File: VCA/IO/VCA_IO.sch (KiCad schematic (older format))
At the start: 15 parts, among them J1 Out_B, J10 IO_B, J11 Power, J2 CV1_B, J3 In_B, J4 CV2_B, J5 IO_A, J6 CV1_A, J7 In_A, J8 CV2_A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

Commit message: Bunch of bug fixes and tweaks
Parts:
- added H1: Top_MH1, Eurorack:eurorack_mounting_hole, symbol Mechanical:MountingHole_Pad
- added H2: Bottom_MH1, Eurorack:eurorack_mounting_hole, symbol Mechanical:MountingHole_Pad
- added H3: Top_MH2, Eurorack:eurorack_mounting_hole, symbol Mechanical:MountingHole_Pad
- added H4: Bottom_MH2, Eurorack:eurorack_mounting_hole, symbol Mechanical:MountingHole_Pad
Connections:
- net GNDREF: now also H1.1, H2.1, H3.1, H4.1
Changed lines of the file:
@@
 EESchema Schematic File Version 4
-LIBS:AS3360_VCA-cache
-EELAYER 29 0
+LIBS:VCA_IO-cache
+EELAYER 30 0
 EELAYER END
 $Descr A4 11693 8268
@@
 Wire Wire Line
 	8800 2950 8800 3300
+$Comp
+L Mechanical:MountingHole_Pad H1
+U 1 1 5D9303C3
+P 8650 950
+F 0 "H1" H 8750 999 50  0000 L CNN
+F 1 "Top_MH1" H 8750 908 50  0000 L CNN
+F 2 "Eurorack:eurorack_mounting_hole" H 8650 950 50  0001 C CNN
+F 3 "~" H 8650 950 50  0001 C CNN
+	1    8650 950
+	1    0    0    -1
+$EndComp
+$Comp
+L power:GNDREF #PWR0109
+U 1 1 5D930ACE
+P 8650 1050
+F 0 "#PWR0109" H 8650 800 50  0001 C CNN
+F 1 "GNDREF" H 8655 877 50  0001 C CNN
+F 2 "" H 8650 1050 50  0001 C CNN
+F 3 "" H 8650 1050 50  0001 C CNN
+	1    8650 1050
+	1    0    0    -1
+$EndComp
+$Comp
+L Mechanical:MountingHole_Pad H3
+U 1 1 5D931B86
+P 9700 950
+F 0 "H3" H 9800 999 50  0000 L CNN
+F 1 "Top_MH2" H 9800 908 50  0000 L CNN
+F 2 "Eurorack:eurorack_mounting_hole" H 9700 950 50  0001 C CNN
+F 3 "~" H 9700 950 50  0001 C CNN
+	1    9700 950
+	1    0    0    -1
+$EndComp
+$Comp
+L power:GNDREF #PWR0115
+U 1 1 5D931B8C
+P 9700 1050
+F 0 "#PWR0115" H 9700 800 50  0001 C CNN
+F 1 "GNDREF" H 9705 877 50  0001 C CNN
+F 2 "" H 9700 1050 50  0001 C CNN
+F 3 "" H 9700 1050 50  0001 C CNN
+	1    9700 1050
+	1    0    0    -1
+$EndComp
+$Comp
+L Mechanical:MountingHole_Pad H2
+U 1 1 5D9344C5
+P 8650 1450
+F 0 "H2" H 8750 1499 50  0000 L CNN
+F 1 "Bottom_MH1" H 8750 1408 50  0000 L CNN
+F 2 "Eurorack:eurorack_mounting_hole" H 8650 1450 50  0001 C CNN
+F 3 "~" H 8650 1450 50  0001 C CNN
+	1    8650 1450
+	1    0    0    -1
+$EndComp
+$Comp
+L power:GNDREF #PWR0116
+U 1 1 5D9344CB
+P 8650 1550
+F 0 "#PWR0116" H 8650 1300 50  0001 C CNN
+F 1 "GNDREF" H 8655 1377 50  0001 C CNN
+F 2 "" H 8650 1550 50  0001 C CNN
+F 3 "" H 8650 1550 50  0001 C CNN
+	1    8650 1550
+	1    0    0    -1
+$EndComp
+$Comp
+L Mechanical:MountingHole_Pad H4
+U 1 1 5D93697C
+P 9700 1450
+F 0 "H4" H 9800 1499 50  0000 L CNN
+F 1 "Bottom_MH2" H 9800 1408 50  0000 L CNN
+F 2 "Eurorack:eurorack_mounting_hole" H 9700 1450 50  0001 C CNN
+F 3 "~" H 9700 1450 50  0001 C CNN
+	1    9700 1450
+	1    0    0    -1
+$EndComp
+$Comp
+L power:GNDREF #PWR0117
+U 1 1 5D936982
+P 9700 1550
+F 0 "#PWR0117" H 9700 1300 50  0001 C CNN
+F 1 "GNDREF" H 9705 1377 50  0001 C CNN
+F 2 "" H 9700 1550 50  0001 C CNN
+F 3 "" H 9700 1550 50  0001 C CNN
+	1    9700 1550
+	1    0    0    -1
+$EndComp
 $EndSCHEMATC

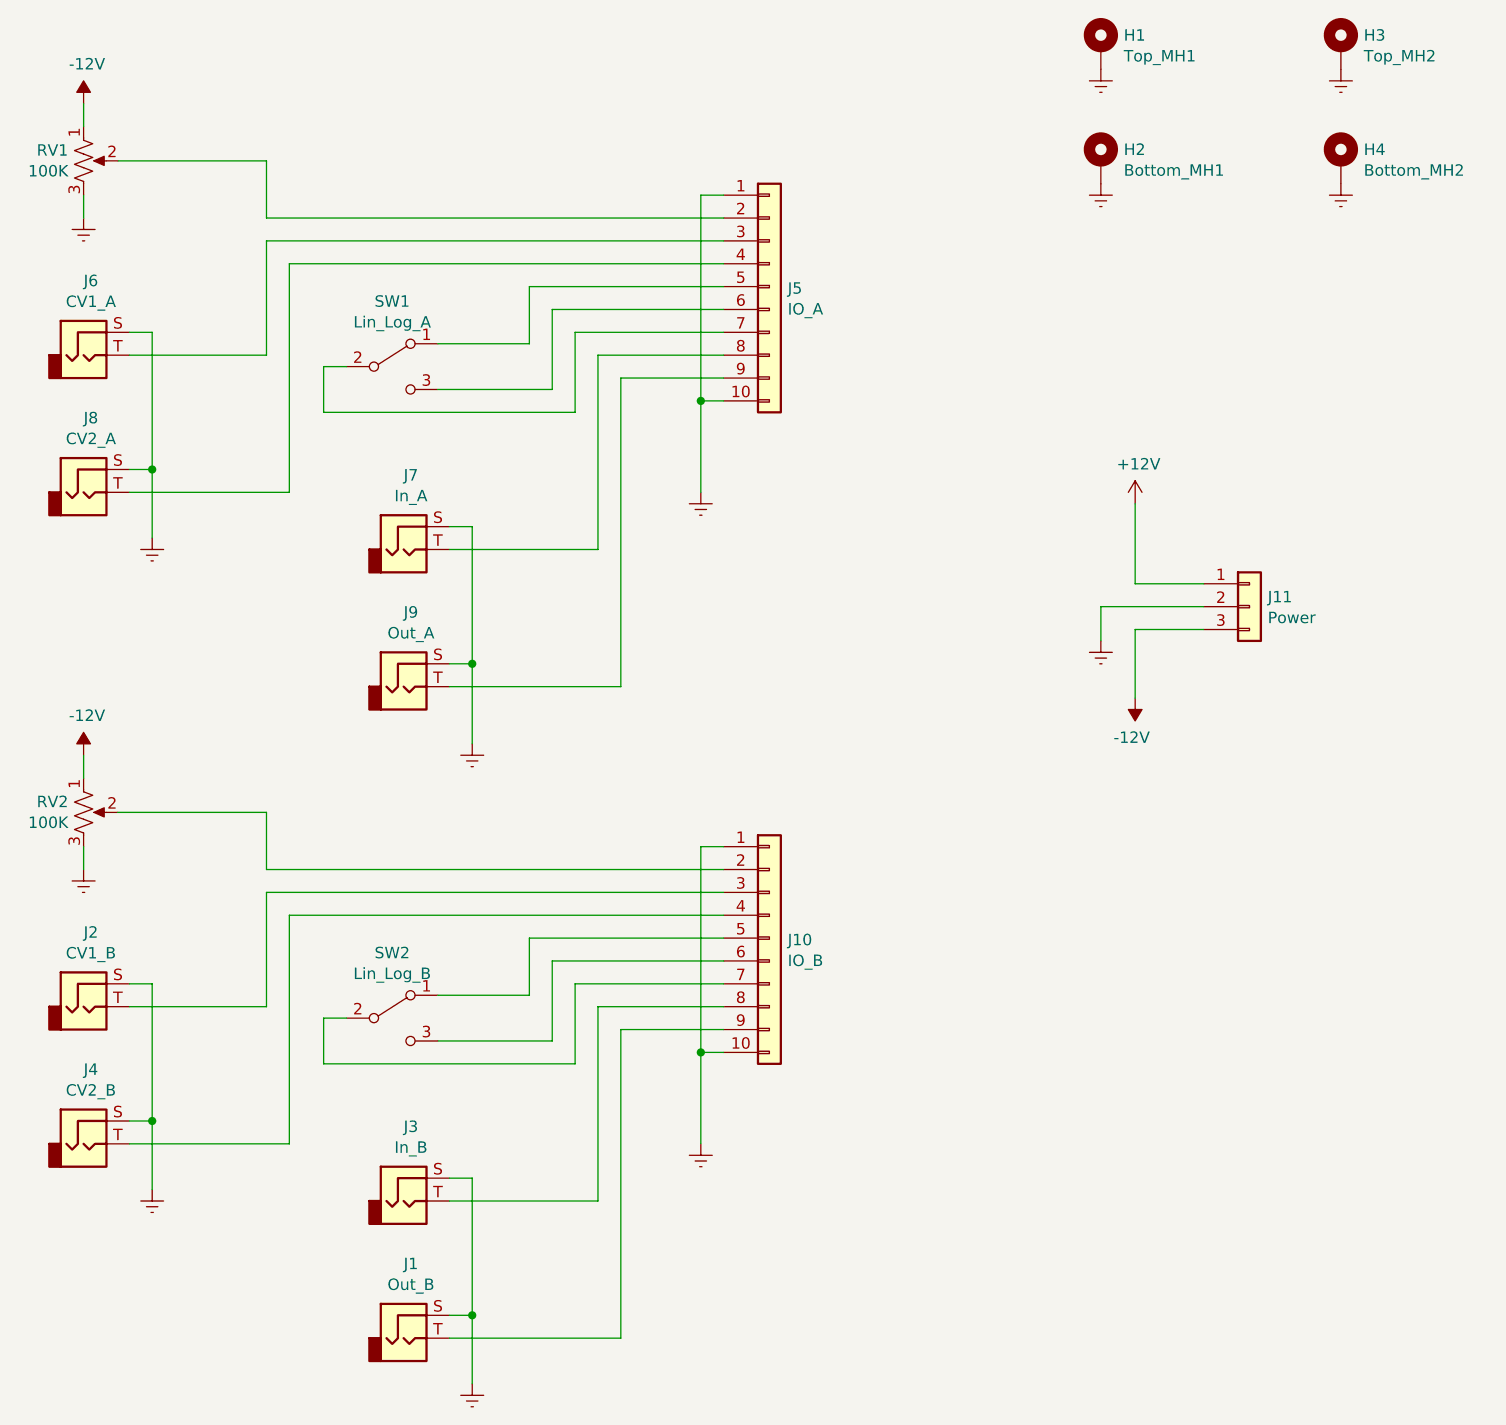
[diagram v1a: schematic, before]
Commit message: Clean up layout of VCA board
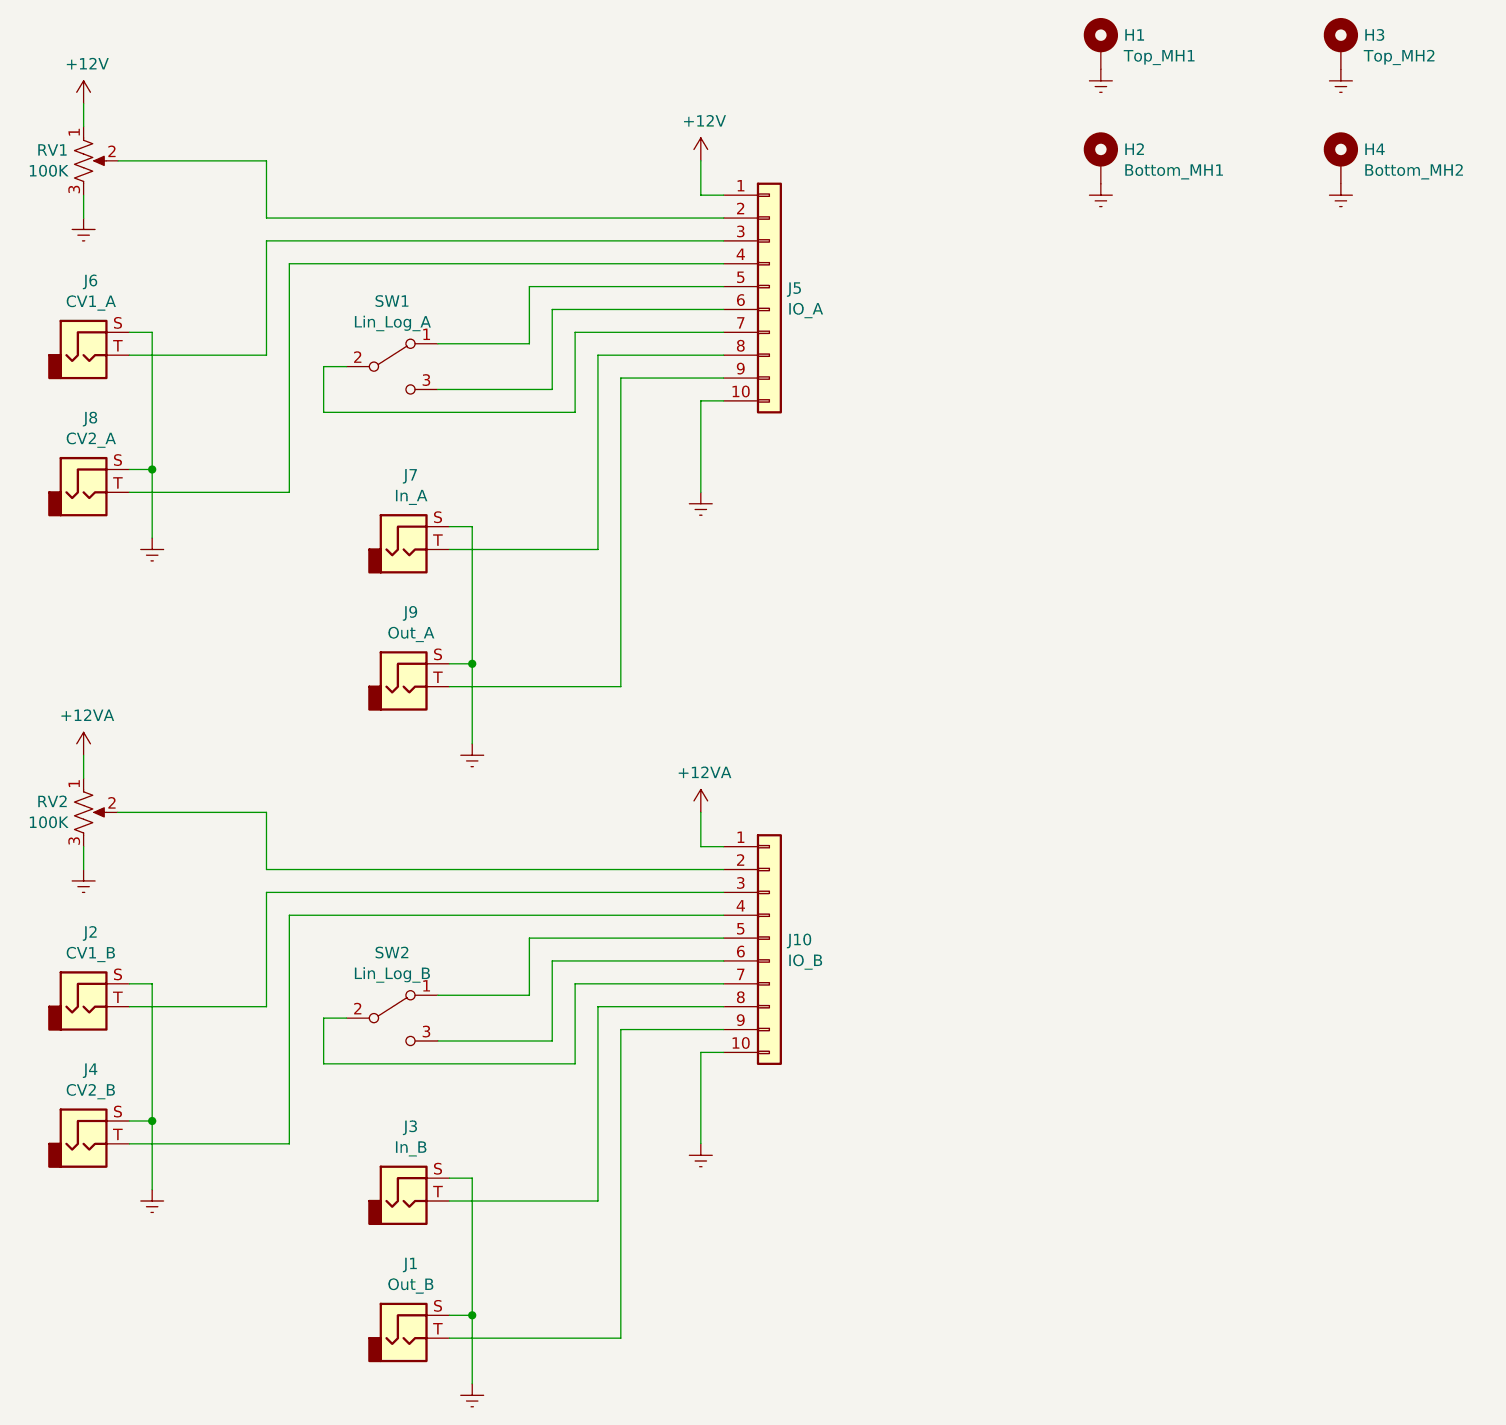
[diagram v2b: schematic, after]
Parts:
- removed J11: Power, Connector_PinSocket_2.54mm:PinSocket_1x03_P2.54mm_Vertical, symbol Connector_Generic:Conn_01x03
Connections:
- net +12V: now also J5.1 (Pin_1), RV1.1
- net GNDREF: no longer J10.1 (Pin_1), J5.1 (Pin_1)
- net -12V renamed +12VA
- net +12VA: now also J10.1 (Pin_1); no longer RV1.1
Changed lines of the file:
@@
 Wire Wire Line
 	4200 1700 4200 1600
-$Comp
-L power:-12V #PWR0102
-U 1 1 5D7C32F9
-P 4200 1200
-F 0 "#PWR0102" H 4200 1300 50  0001 C CNN
-F 1 "-12V" H 4215 1373 50  0000 C CNN
-F 2 "" H 4200 1200 50  0001 C CNN
-F 3 "" H 4200 1200 50  0001 C CNN
-	1    4200 1200
-	1    0    0    -1
-$EndComp
 Wire Wire Line
 	4200 1200 4200 1300
@@
 	1    0    0    -1
 $EndComp
-$Comp
-L power:-12V #PWR0104
-U 1 1 5D7C3EA8
-P 4200 4050
-F 0 "#PWR0104" H 4200 4150 50  0001 C CNN
-F 1 "-12V" H 4215 4223 50  0000 C CNN
-F 2 "" H 4200 4050 50  0001 C CNN
-F 3 "" H 4200 4050 50  0001 C CNN
-	1    4200 4050
-	1    0    0    -1
-$EndComp
-$Comp
-L power:+12V #PWR0106
-U 1 1 5D7C6DCC
-P 8800 2950
-F 0 "#PWR0106" H 8800 2800 50  0001 C CNN
-F 1 "+12V" H 8815 3123 50  0000 C CNN
-F 2 "" H 8800 2950 50  0001 C CNN
-F 3 "" H 8800 2950 50  0001 C CNN
-	1    8800 2950
-	1    0    0    -1
-$EndComp
 Wire Wire Line
 	4200 4450 4200 4550
@@
 	6900 1600 7000 1600
 Wire Wire Line
-	9100 3500 8800 3500
-Wire Wire Line
-	8800 3500 8800 3800
-$Comp
-L power:-12V #PWR0105
-U 1 1 5D8742CF
-P 8800 3800
-F 0 "#PWR0105" H 8800 3900 50  0001 C CNN
-F 1 "-12V" H 8815 3973 50  0000 C CNN
-F 2 "" H 8800 3800 50  0001 C CNN
-F 3 "" H 8800 3800 50  0001 C CNN
-	1    8800 3800
-	-1   0    0    1
-$EndComp
-Wire Wire Line
 	4350 4300 5000 4300
 Wire Wire Line
@@
 Connection ~ 5900 6500
 $Comp
-L Connector_Generic:Conn_01x03 J11
-U 1 1 5D8D6E2F
-P 9300 3400
-F 0 "J11" H 9380 3442 50  0000 L CNN
-F 1 "Power" H 9380 3351 50  0000 L CNN
-F 2 "Connector_PinSocket_2.54mm:PinSocket_1x03_P2.54mm_Vertical" H 9300 3400 50  0001 C CNN
-F 3 "~" H 9300 3400 50  0001 C CNN
-	1    9300 3400
-	1    0    0    -1
-$EndComp
-$Comp
 L Connector_Generic:Conn_01x10 J5
 U 1 1 5D8DEBA8
@@
 	1    0    0    -1
 $EndComp
-Connection ~ 6900 2500
-Wire Wire Line
-	6900 2500 6900 1600
 Wire Wire Line
 	6900 2500 6900 2900
@@
 	1    0    0    -1
 $EndComp
-Connection ~ 6900 5350
-Wire Wire Line
-	6900 5350 6900 4450
 Wire Wire Line
 	6900 5350 6900 5750
@@
 $EndComp
 $Comp
-L power:GNDREF #PWR0108
-U 1 1 5D907247
-P 8650 3550
-F 0 "#PWR0108" H 8650 3300 50  0001 C CNN
-F 1 "GNDREF" H 8655 3377 50  0001 C CNN
-F 2 "" H 8650 3550 50  0001 C CNN
-F 3 "" H 8650 3550 50  0001 C CNN
-	1    8650 3550
-	1    0    0    -1
-$EndComp
-Wire Wire Line
-	8650 3550 8650 3400
-Wire Wire Line
-	8650 3400 9100 3400
-Wire Wire Line
-	8800 3300 9100 3300
-Wire Wire Line
-	8800 2950 8800 3300
-$Comp
 L Mechanical:MountingHole_Pad H1
 U 1 1 5D9303C3
@@
 	1    0    0    -1
 $EndComp
+$Comp
+L power:+12V #PWR0102
+U 1 1 5D9DB15B
+P 4200 1200
+F 0 "#PWR0102" H 4200 1050 50  0001 C CNN
+F 1 "+12V" H 4215 1373 50  0000 C CNN
+F 2 "" H 4200 1200 50  0001 C CNN
+F 3 "" H 4200 1200 50  0001 C CNN
+	1    4200 1200
+	1    0    0    -1
+$EndComp
+Wire Wire Line
+	6900 4450 6900 4300
+$Comp
+L power:+12V #PWR0106
+U 1 1 5D9E4A91
+P 6900 1450
+F 0 "#PWR0106" H 6900 1300 50  0001 C CNN
+F 1 "+12V" H 6915 1623 50  0000 C CNN
+F 2 "" H 6900 1450 50  0001 C CNN
+F 3 "" H 6900 1450 50  0001 C CNN
+	1    6900 1450
+	1    0    0    -1
+$EndComp
+Wire Wire Line
+	6900 1450 6900 1600
+$Comp
+L power:+12VA #PWR?
+U 1 1 5D9F3DB9
+P 6900 4300
+F 0 "#PWR?" H 6900 4150 50  0001 C CNN
+F 1 "+12VA" H 6915 4473 50  0000 C CNN
+F 2 "" H 6900 4300 50  0001 C CNN
+F 3 "" H 6900 4300 50  0001 C CNN
+	1    6900 4300
+	1    0    0    -1
+$EndComp
+$Comp
+L power:+12VA #PWR?
+U 1 1 5D9F9FC1
+P 4200 4050
+F 0 "#PWR?" H 4200 3900 50  0001 C CNN
+F 1 "+12VA" H 4215 4223 50  0000 C CNN
+F 2 "" H 4200 4050 50  0001 C CNN
+F 3 "" H 4200 4050 50  0001 C CNN
+	1    4200 4050
+	1    0    0    -1
+$EndComp

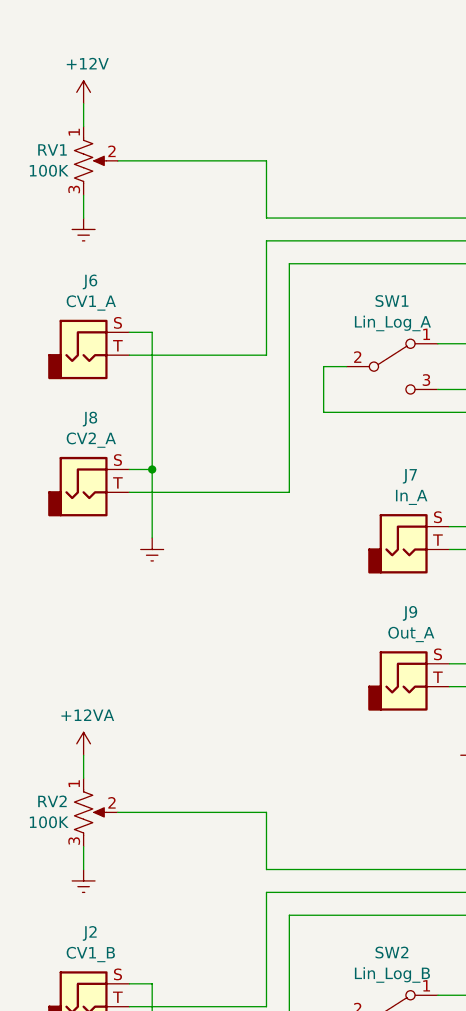
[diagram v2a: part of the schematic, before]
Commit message: Fix backwards knobs
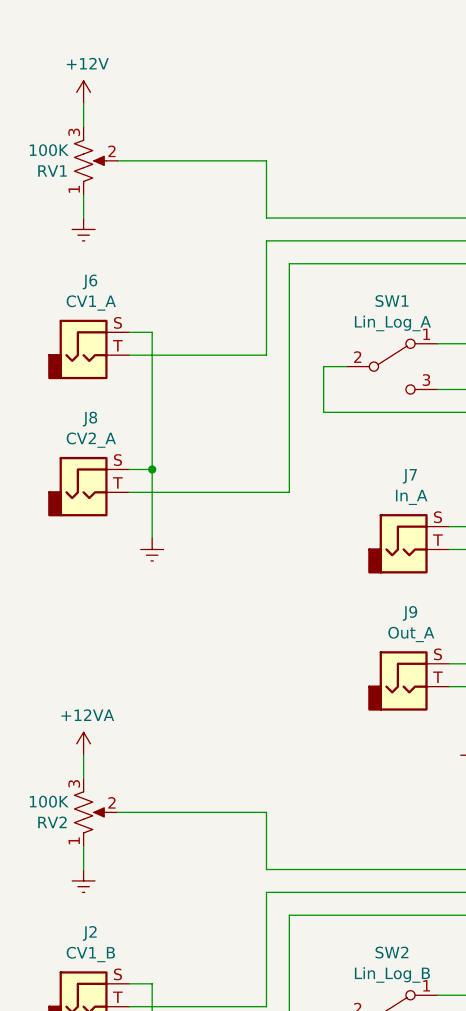
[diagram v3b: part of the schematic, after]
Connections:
- net +12V: now also RV1.3; no longer RV1.1
- net +12VA: now also RV2.3; no longer RV2.1
- net GNDREF: now also RV1.1, RV2.1; no longer RV1.3, RV2.3
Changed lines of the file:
@@
 F 3 "~" H 4200 1450 50  0001 C CNN
 	1    4200 1450
-	1    0    0    -1
+	1    0    0    1
 $EndComp
 $Comp
@@
 F 3 "~" H 4200 4300 50  0001 C CNN
 	1    4200 4300
-	1    0    0    -1
+	1    0    0    1
 $EndComp
 $Comp
